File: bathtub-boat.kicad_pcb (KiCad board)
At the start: 2 copper layers, 59.3 x 34 mm, 33 parts, among them J1 I2C, J2 SPI, J3 I2C, J4 DS18B20, SW1 MODE, SW2 RESET, SW3 POWER, SW4 A, U1 esp-01m, U2 tp4056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

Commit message: Prepare for milling
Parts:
- added C1: C_Polarized_Small, Capacitor_THT:CP_Radial_D5.0mm_P2.50mm, F.Cu at (139.7, 75.0)
- added C2: C_Polarized_Small, Capacitor_THT:CP_Radial_D5.0mm_P2.50mm, F.Cu at (137.5, 88.5)
- added kibuzzard-65B795B9: G***, kibuzzard-65B795B9, F.Cu at (129.0, 102.5)
- moved kibuzzard-65B795B9 7.91 mm to (140.5, 84.5)
- moved kibuzzard-65B8C65E 6.47 mm to (136.0, 92.5)
- moved D1 5.03 mm to (140.2, 82.5), turned to 180 degrees
- moved J4 1.79 mm to (138.0, 97.5)
- moved U6 0.57 mm to (113.1, 93.4)
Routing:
- net Neopixel: track 21.0 -> 16.5 mm
- net VBUS: track 36.4 -> 40.9 mm
- net unconnected-(D1-Pad2): track 4.03 -> 0.00 mm, vias 1 -> 0
- net Temp: track 14.9 -> 16.8 mm
- net +5V: track 28.5 -> 27.8 mm
- net +3V3: track 106.8 -> 107.4 mm

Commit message: Production ready
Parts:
- moved J1 0.08 mm to (124.5, 96.8)
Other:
- rule pad_to_mask_clearance: 0 -> 0.05
- board text added: "PCB_3D_BR"
- board text added: "PCB_3D_TL"
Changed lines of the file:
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@@
       (dielectric_constraints no)
     )
-    (pad_to_mask_clearance 0)
+    (pad_to_mask_clearance 0.05)
     (aux_axis_origin 100 100)
     (grid_origin 141.5 94.5)
@@
   )
   (footprint "Connector_JST:JST_SH_SM04B-SRSS-TB_1x04-1MP_P1.00mm_Horizontal" (layer "B.Cu")
-    (at 124.423322 96.797887 180)
+    (at 124.5 96.797887 180)
     (descr "JST SH series connector, SM04B-SRSS-TB (http://www.jst-mfg.com/product/pdf/eng/eSH.pdf), generated with kicad-footprint-generator")
     (tags "connector JST SH top entry")
@@
     (pad "4" smd roundrect (at 1.5 2 180) (size 0.8 2) (drill (offset 0.4 0)) (layers "B.Cu" "B.Paste" "B.Mask") (roundrect_rratio 0.25)
       (net 13 "I2C_SCL") (pinfunction "Pin_4") (pintype "passive"))
-    (pad "MP" smd roundrect (at -2.8 -1.875 180) (size 1.2 1.8) (layers "B.Cu" "B.Paste" "B.Mask") (roundrect_rratio 0.208333))
-    (pad "MP" smd roundrect (at 2.8 -1.875 180) (size 1.2 1.8) (layers "B.Cu" "B.Paste" "B.Mask") (roundrect_rratio 0.208333))
+    (pad "MP" smd roundrect (at -2.8 -1.875 180) (size 1.2 1.8) (layers "B.Cu" "B.Paste" "B.Mask") (roundrect_rratio 0.2083333333))
+    (pad "MP" smd roundrect (at 2.8 -1.875 180) (size 1.2 1.8) (layers "B.Cu" "B.Paste" "B.Mask") (roundrect_rratio 0.2083333333))
     (model "${KICAD6_3DMODEL_DIR}/Connector_JST.3dshapes/JST_SH_SM04B-SRSS-TB_1x04-1MP_P1.00mm_Horizontal.wrl"
       (offset (xyz 0 0 0))
@@
     (effects (font (size 1.2 1.2) (thickness 0.2)))
   )
+  (gr_text "PCB_3D_TL" (at 103.908 66.56) (layer "User.1")
+    (effects (font (size 1 1) (thickness 0.15)))
+  )
+  (gr_text "PCB_3D_BR" (at 155.216 99.58) (layer "User.1")
+    (effects (font (size 1 1) (thickness 0.15)))
+  )
   (segment (start 103.762589 83.410293) (end 103.762589 85.362589) (width 0.4) (layer "B.Cu") (net 1))
   (segment (start 147.118 84.318) (end 146.836 84.6) (width 0.4) (layer "B.Cu") (net 1))
@@
   (segment (start 135.233229 89.110084) (end 135.225756 89.110084) (width 0.8) (layer "B.Cu") (net 3))
   (segment (start 129.5 80.9) (end 129.4 80.8) (width 0.8) (layer "B.Cu") (net 3))
-  (segment (start 129.4 80.8) (end 129 80.4) (width 0.8) (layer "B.Cu") (net 3))
   (segment (start 116.2375 78.6975) (end 116.04 78.5) (width 0.4) (layer "B.Cu") (net 3))
+  (segment (start 127.5 78.9) (end 127.5 73.5) (width 0.8) (layer "B.Cu") (net 3))
+  (segment (start 127.5 73.5) (end 128 73) (width 0.8) (layer "B.Cu") (net 3))
   (segment (start 138 91.876855) (end 136.823145 90.7) (width 0.8) (layer "B.Cu") (net 3))
   (segment (start 135.225756 89.110084) (end 129.5 83.384328) (width 0.8) (layer "B.Cu") (net 3))
@@
   (segment (start 112.903768 72.991764) (end 112.912004 73) (width 0.8) (layer "B.Cu") (net 3))
   (segment (start 129.5 83.384328) (end 129.5 80.9) (width 0.8) (layer "B.Cu") (net 3))
-  (segment (start 129 74) (end 128 73) (width 0.8) (layer "B.Cu") (net 3))
   (segment (start 103.762589 75.790293) (end 105.209707 75.790293) (width 0.8) (layer "B.Cu") (net 3))
+  (segment (start 129.4 80.8) (end 127.5 78.9) (width 0.8) (layer "B.Cu") (net 3))
   (segment (start 110.905105 72.991764) (end 112.903768 72.991764) (width 0.8) (layer "B.Cu") (net 3))
   (segment (start 152.2 86.88) (end 152.2 89) (width 0.8) (layer "B.Cu") (net 3))
   (segment (start 135.889916 89.110084) (end 136.5 88.5) (width 0.8) (layer "B.Cu") (net 3))
-  (segment (start 129 80.4) (end 129 74) (width 0.8) (layer "B.Cu") (net 3))
   (segment (start 126.21 90.080069) (end 126.440069 89.85) (width 0.6) (layer "B.Cu") (net 3))
   (segment (start 116.2375 81) (end 116.2375 78.6975) (width 0.4) (layer "B.Cu") (net 3))
@@
   (segment (start 125.7625 72.763333) (end 127.275335 71.250498) (width 0.4) (layer "B.Cu") (net 7))
   (segment (start 130.850498 71.250498) (end 132.2 72.6) (width 0.4) (layer "B.Cu") (net 7))
-  (segment (start 141.064056 94.785944) (end 119.664055 94.785944) (width 0.4) (layer "F.Cu") (net 8))
-  (segment (start 143.2 92.65) (end 141.064056 94.785944) (width 0.4) (layer "F.Cu") (net 8))
+  (segment (start 141.064056 94.785944) (end 119.664055 94.785944) (width 0.8) (layer "F.Cu") (net 8))
+  (segment (start 143.2 92.65) (end 141.064056 94.785944) (width 0.8) (layer "F.Cu") (net 8))
   (via (at 143.2 92.65) (size 1.5) (drill 1.1) (layers "F.Cu" "B.Cu") (net 8))
   (via (at 119.664055 94.785944) (size 1.5) (drill 1.1) (layers "F.Cu" "B.Cu") (net 8))

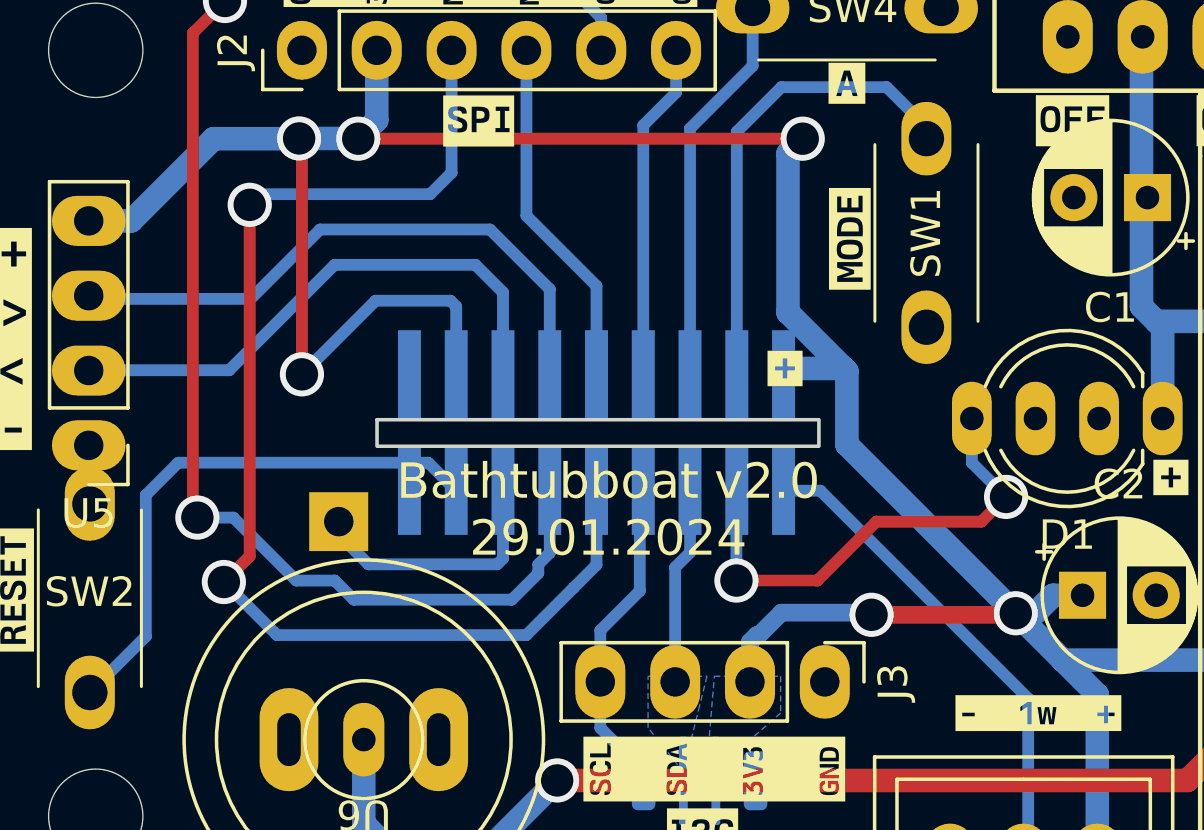
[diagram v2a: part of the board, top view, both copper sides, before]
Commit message: Add pullup resistor for optional parasitic power
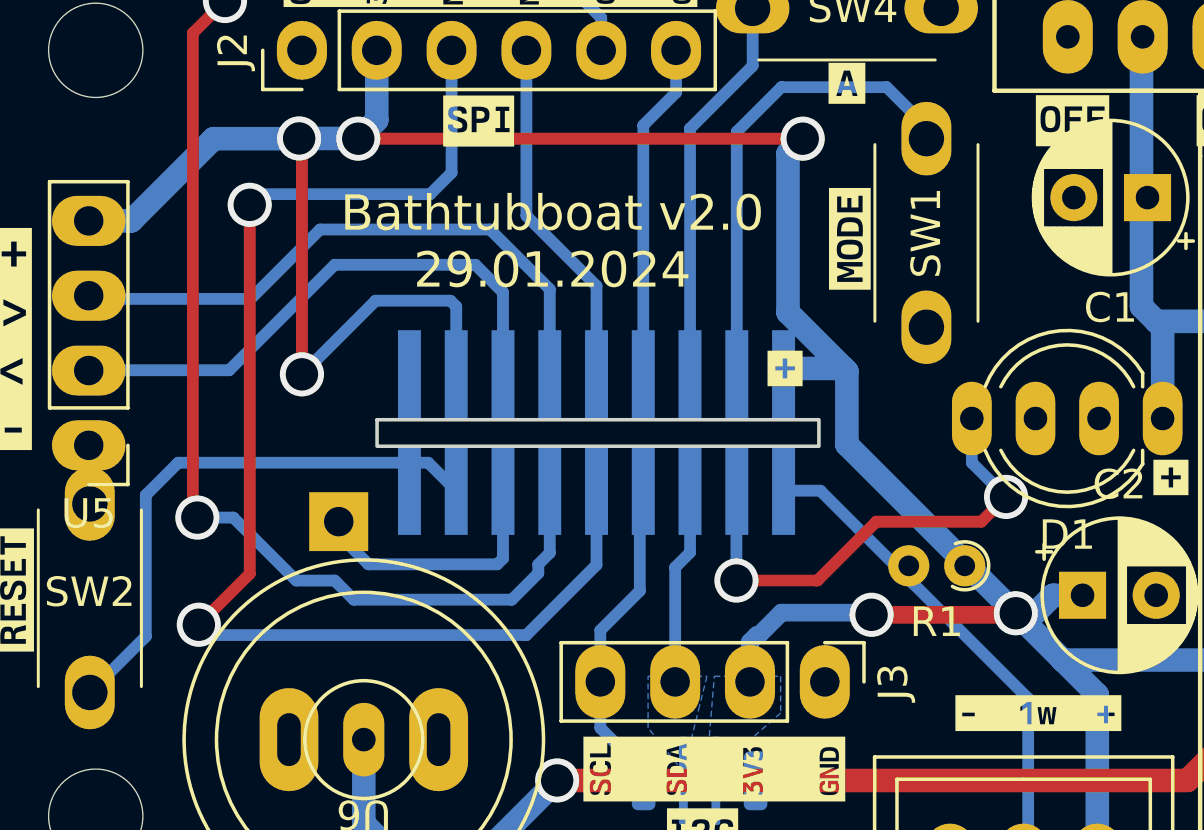
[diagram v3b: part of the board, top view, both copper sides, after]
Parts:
- added R1: 47k, Resistor_THT:R_Axial_DIN0204_L3.6mm_D1.6mm_P1.90mm_Vertical, F.Cu at (133.5, 87.5)
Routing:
- net SPI_MISO: track 41.5 -> 43.6 mm
- net +3V3: track 107.8 -> 108.6 mm
- net Temp: track 16.8 -> 17.5 mm

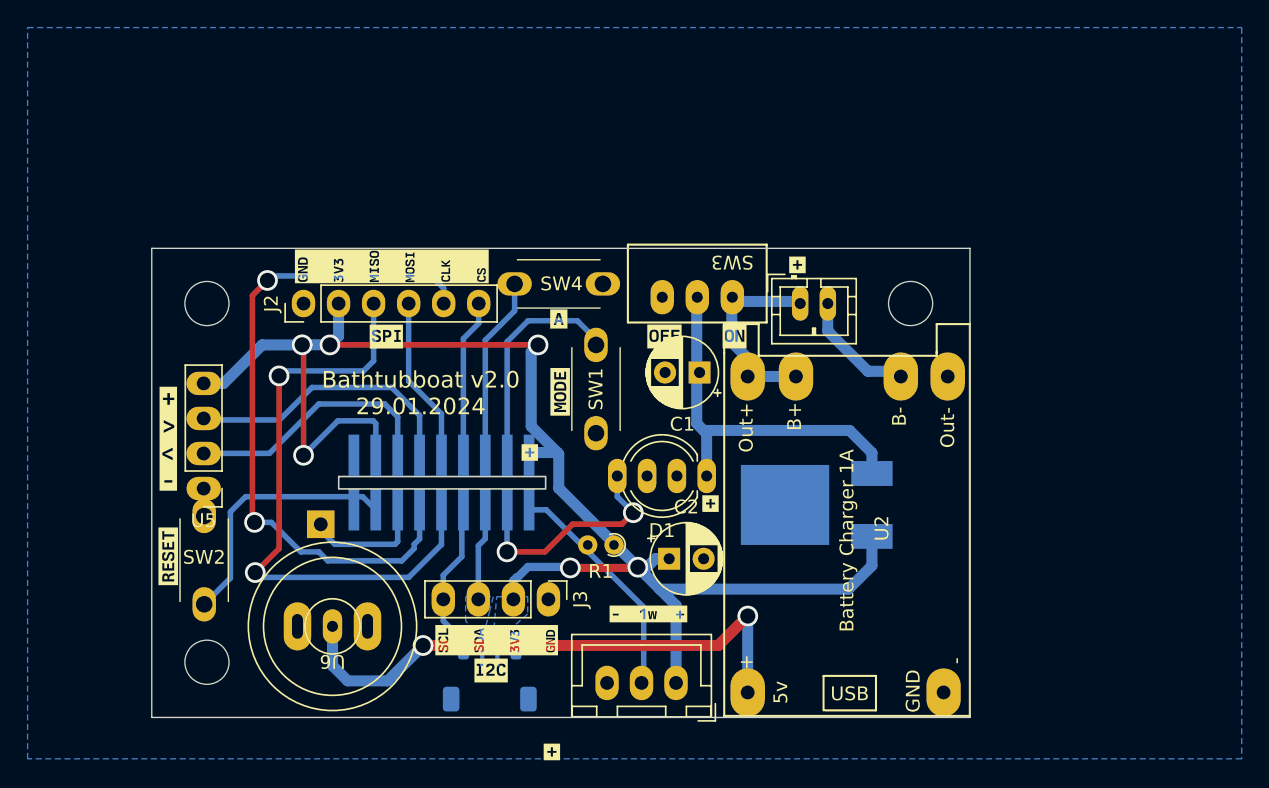
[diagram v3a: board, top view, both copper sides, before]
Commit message: Update Silkscreen
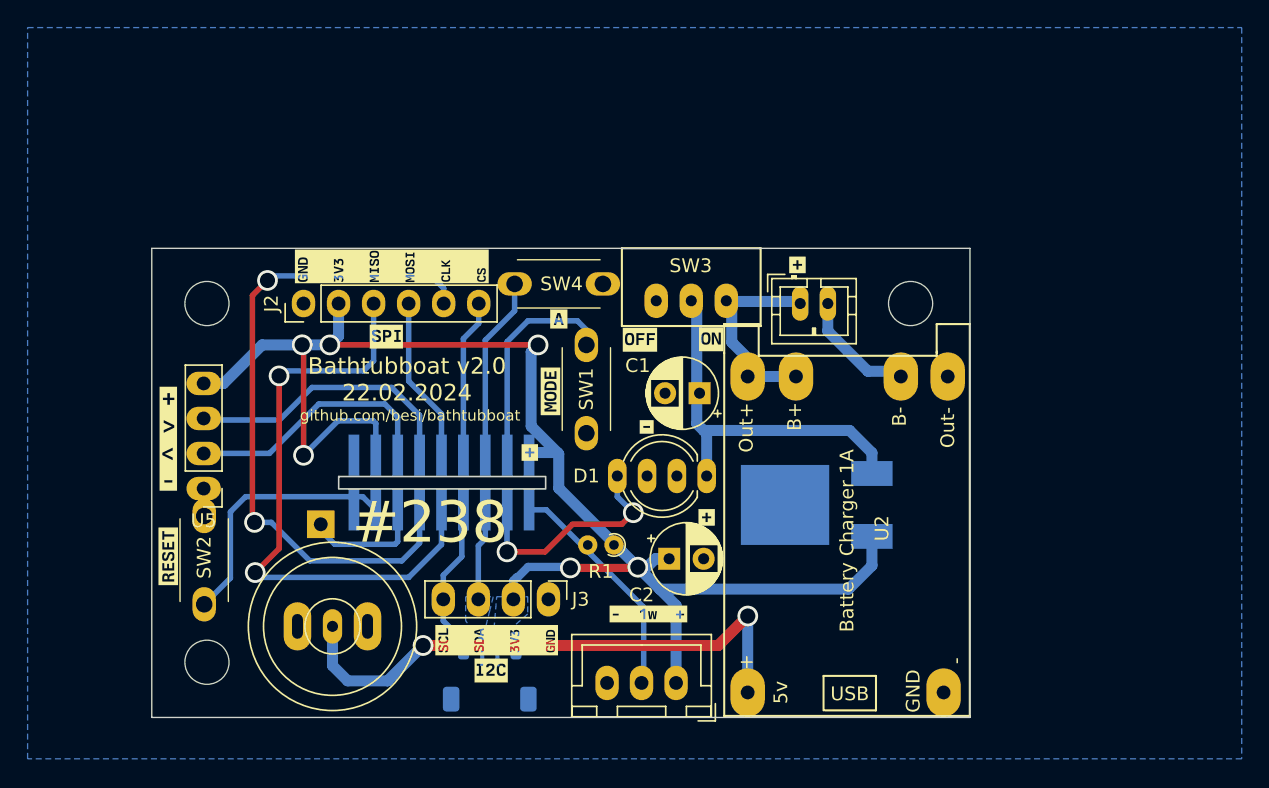
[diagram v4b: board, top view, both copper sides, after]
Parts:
- removed the kibuzzard-65B795B9 at (129.0, 102.5)
- added G***: LOGO, LOGO, B.Cu at (150.5, 94.5)
- added kibuzzard-65D6F389: G***, kibuzzard-65D6F389, F.Cu at (135.9, 78.9)
- moved kibuzzard-65B98083 1.79 mm to (135.4, 72.6)
- moved kibuzzard-65B98079 1.72 mm to (140.5, 72.6)
- moved C1 1.50 mm to (139.7, 76.5)
- moved kibuzzard-65B795B9 1.04 mm to (140.2, 85.5)
- moved kibuzzard-65B7959E 0.70 mm to (128.9, 76.4)
- moved SW1 0.70 mm to (131.5, 79.4)
- moved SW3 0.51 mm to (136.6, 69.8)
- turned U6 to 0 degrees
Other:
- board text added: "#238"
- board text added: "Bathtubboat v2.0 22.02.2024"
- board text added: "JLC:"
- board text added: "JLCJLCJLCJLC"
- board text added: "github.com/besi/bathtubboat"
- board text removed: "Bathtubboat v2.0 29.01.2024"

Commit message: Add a top copper pour
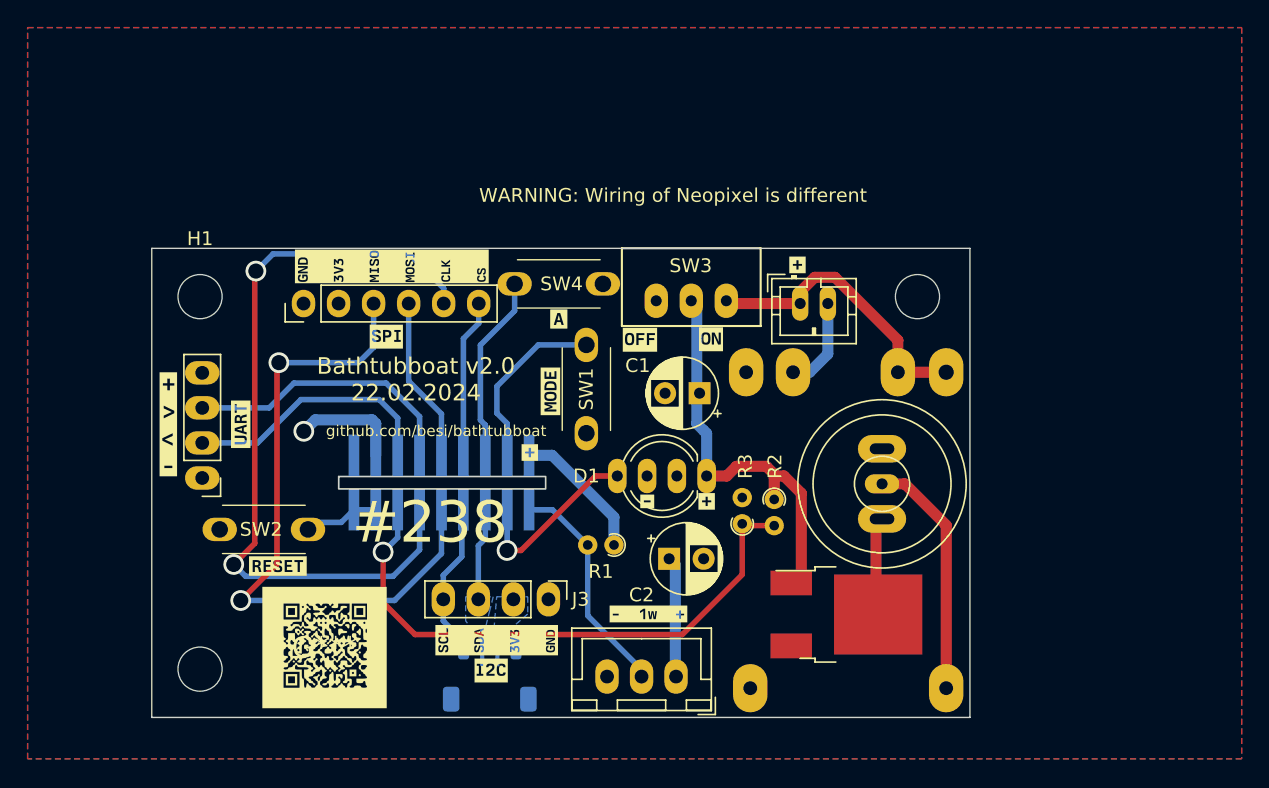
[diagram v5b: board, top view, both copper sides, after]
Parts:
- removed the G*** at (150.5, 94.5)
- removed TP1: ADC, TestPoint:TestPoint_THTPad_2.0x2.0mm_Drill1.0mm
- added G***: LOGO, LOGO, F.Cu at (112.5, 94.9)
- added G***: LOGO, LOGO, B.Cu at (114.9, 91.8)
- added R2: 100k, Resistor_THT:R_Axial_DIN0204_L3.6mm_D1.6mm_P1.90mm_Vertical, F.Cu at (145.1, 84.2)
- added R3: 100k, Resistor_THT:R_Axial_DIN0204_L3.6mm_D1.6mm_P1.90mm_Vertical, F.Cu at (142.8, 86.0)
- added kibuzzard-65B79508: G***, kibuzzard-65B79508, B.Cu at (125.0, 89.4)
- added kibuzzard-65B79597: G***, kibuzzard-65B79597, B.Cu at (108.2, 85.0)
- added kibuzzard-65B7959E: G***, kibuzzard-65B7959E, B.Cu at (131.3, 76.4)
- added kibuzzard-65B795B9: G***, kibuzzard-65B795B9, B.Cu at (146.8, 67.2)
- added kibuzzard-65B7965E: G***, kibuzzard-65B7965E, B.Cu at (101.2, 78.8)
- added kibuzzard-65B796EF: G***, kibuzzard-65B796EF, B.Cu at (128.1, 87.3)
- added kibuzzard-65B796FD: G***, kibuzzard-65B796FD, B.Cu at (117.0, 72.4)
- added kibuzzard-65B8C3A2: G***, kibuzzard-65B8C3A2, B.Cu at (117.4, 67.3)
- added kibuzzard-65B8C65E: G***, kibuzzard-65B8C65E, B.Cu at (135.6, 94.6)
- added kibuzzard-65D7C44D: G***, kibuzzard-65D7C44D, F.Cu at (106.4, 78.8)
- added kibuzzard-65D7C44D: G***, kibuzzard-65D7C44D, B.Cu at (106.4, 78.8)
- U2: moved to B.Cu
- U3: moved to F.Cu
- moved U6 41.1 mm to (152.9, 83.1), turned to 90 degrees
- moved U3 8.34 mm to (150.5, 92.5), turned to 0 degrees
- moved kibuzzard-65B79597 7.98 mm to (109.1, 89.0), turned to 0 degrees
- moved kibuzzard-65D6F389 5.40 mm to (135.9, 84.3)
- moved SW2 1.49 mm to (104.9, 86.4), turned to 0 degrees
- moved kibuzzard-65B795B9 1.16 mm to (140.2, 84.3)
- moved kibuzzard-65B7965E 1.05 mm to (101.2, 78.8)
- moved U5 0.77 mm to (103.7, 82.6)
- moved H1 0.71 mm to (103.5, 69.5)
- moved H2 0.71 mm to (155.5, 69.5)
- moved H3 0.71 mm to (103.5, 96.5)
- moved J4 0.46 mm to (138.0, 97.0)
- moved U2 0.31 mm to (150.4, 86.9)
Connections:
- U1 pad 16: Net-(TP1-Pad1) -> ADC
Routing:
- net +3V3: track 108.6 -> 27.0 mm, vias 6 -> 1
- net ADC: track 0.00 -> 42.0 mm, vias 0 -> 1
- net VBUS: track 40.9 -> 17.7 mm, vias 2 -> 0
- net Net-(U1-GP16): track 18.9 -> 5.50 mm
- net Net-(TP1-Pad1): track 8.82 -> 0.00 mm
- net SPI_CLK: track 48.5 -> 55.7 mm
- net /BAT+: track 15.1 -> 21.5 mm, vias 0 -> 1
- net SPI_MISO: track 43.6 -> 48.0 mm
- net GND: track 3.34 -> 7.18 mm
- net Neopixel: track 16.5 -> 13.2 mm, vias 2 -> 1
- net Net-(U1-GP0): track 16.0 -> 13.0 mm
- net +5V: track 27.6 -> 30.0 mm
- net /BAT-: track 8.65 -> 6.73 mm
- net Temp: track 17.5 -> 16.5 mm
- added copper zone on F.Cu, net +3V3
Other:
- board text added: "WARNING: Wiring of Neopixel is different"

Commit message: Round corners some silkscreen cleanup and a TRS Plug for the 1Wire connection
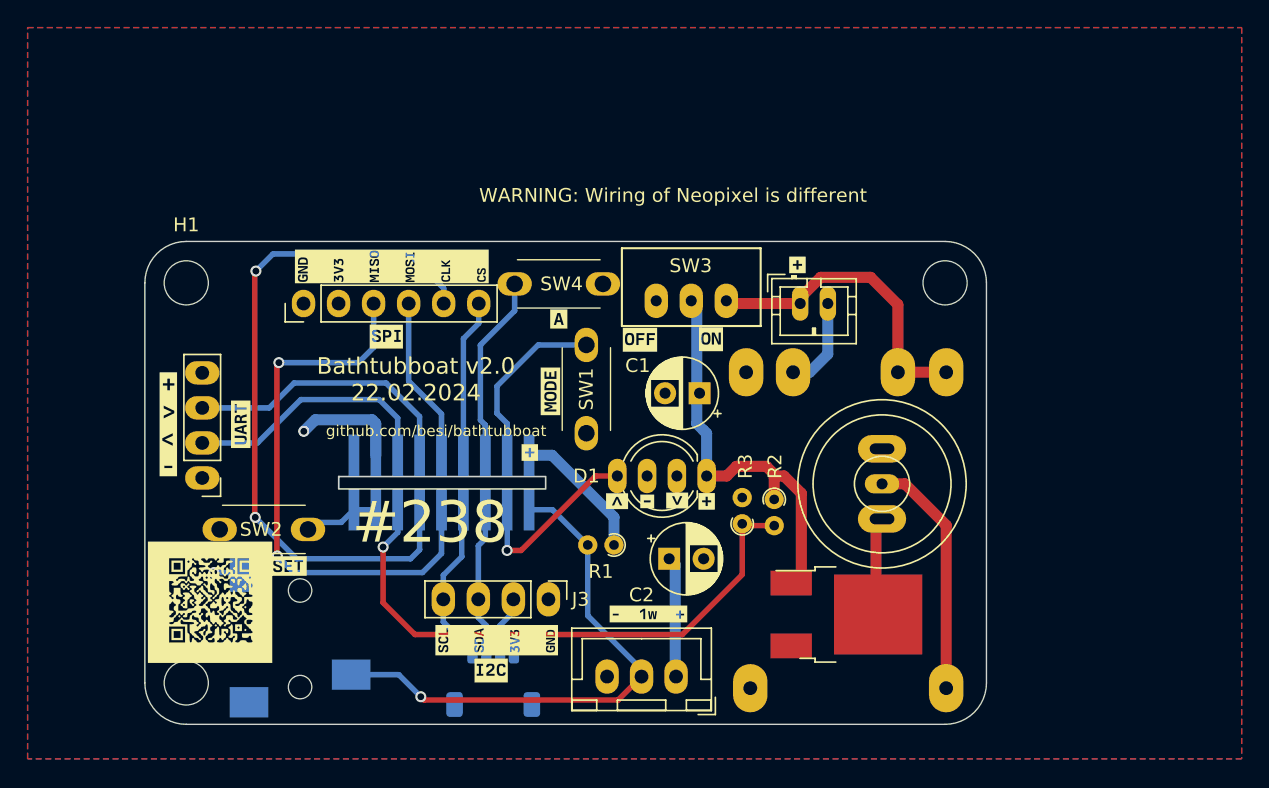
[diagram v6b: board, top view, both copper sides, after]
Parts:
- added J5: 1WireTRS, Connector_Audio:Jack_3.5mm_CUI_SJ-3523-SMT_Horizontal, B.Cu at (110.8, 95.3)
- added kibuzzard-679F7FF7: G***, kibuzzard-679F7FF7, F.Cu at (138.1, 84.3)
- added kibuzzard-679F7FF7: G***, kibuzzard-679F7FF7, F.Cu at (133.7, 84.3)
- R3: value 100k -> TODO Add Light meter here
- moved G*** 8.92 mm to (104.2, 91.7)
- moved H2 2.24 mm to (157.5, 68.5)
- moved H1 1.41 mm to (102.5, 68.5)
- moved H3 1.41 mm to (102.5, 97.5)
- moved G*** 0.66 mm to (115.5, 91.5)
- moved J1 0.46 mm to (124.7, 97.2)
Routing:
- net Temp: track 16.5 -> 39.0 mm, vias 0 -> 1
- net SPI_MISO: track 48.0 -> 40.7 mm
- net +3V3: track 27.0 -> 33.7 mm, vias 1 -> 2
- net SPI_CLK: track 55.7 -> 50.5 mm
- net I2C_SDA: track 6.78 -> 10.8 mm
- net /BAT+: track 21.5 -> 22.8 mm, vias 1 -> 0
- net I2C_SCL: track 10.9 -> 11.7 mm
- removed copper zone on B.Cu, net +3V3
- removed copper zone on B.Cu, net I2C_SDA
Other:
- board size 59.3 x 34 mm -> 61 x 35 mm
- board text removed: "JLC:"
- board text removed: "JLCJLCJLCJLC"
